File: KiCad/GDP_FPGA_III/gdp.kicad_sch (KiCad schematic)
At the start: 39 parts, among them J1 NKC-Bus, J2 Mini-DIN-6, J3 Mini-DIN-6, J4 AudioJack3, J5 SD_Card, U2 74LVC245, U3 74LVC245, U4 74LVC245

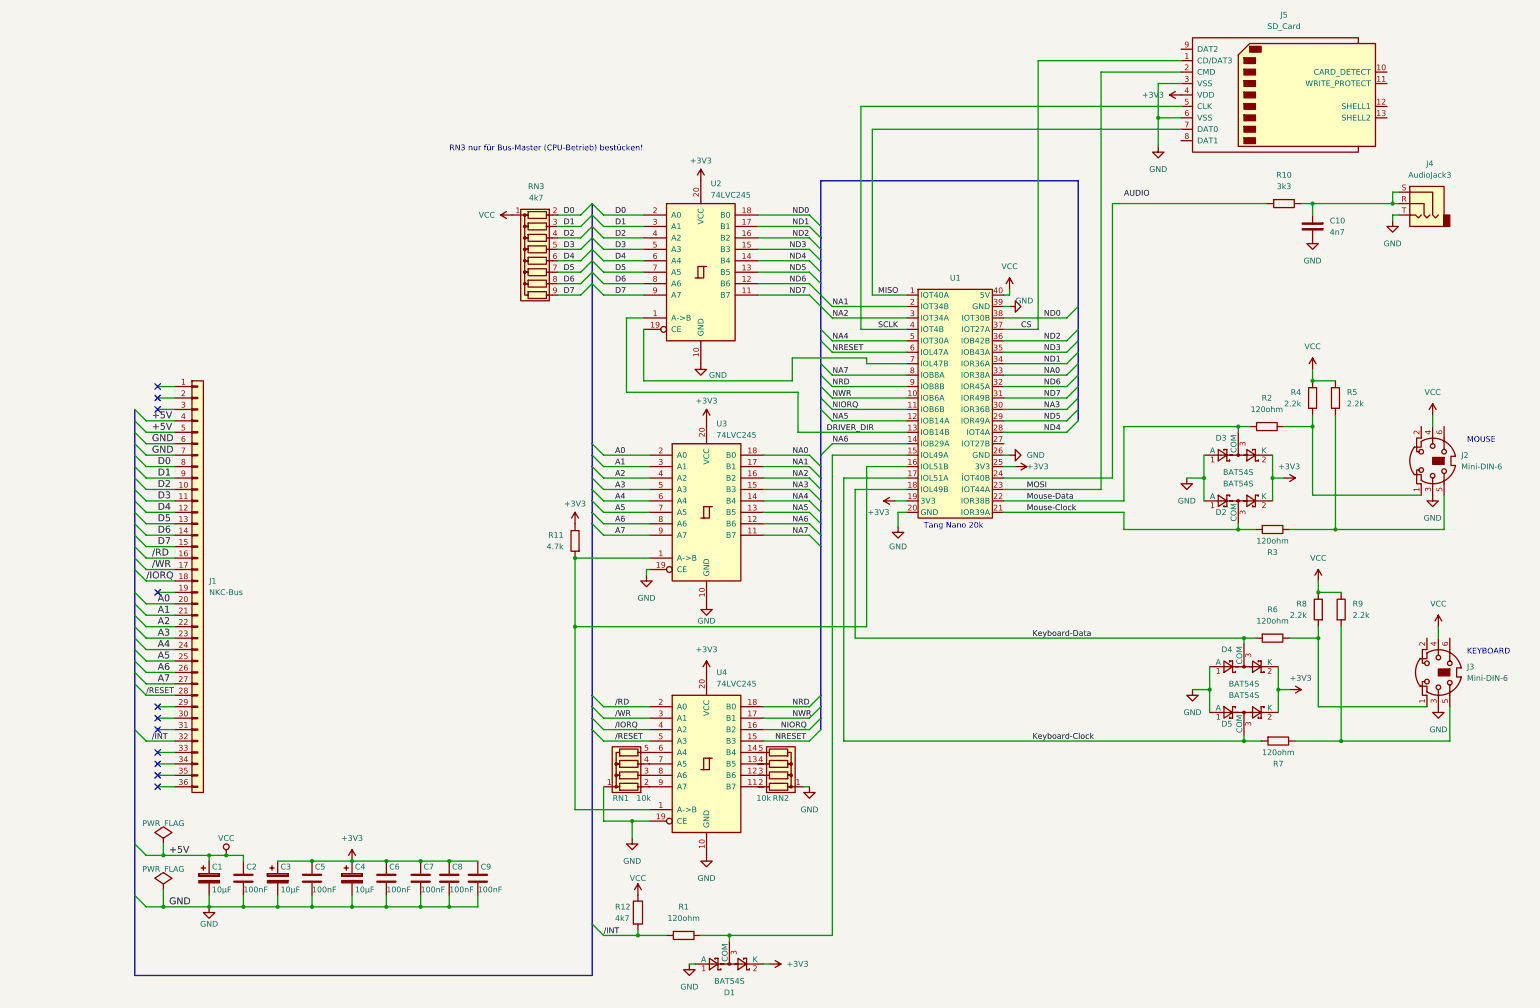
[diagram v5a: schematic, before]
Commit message: update Level shifter to 74LVC8T245
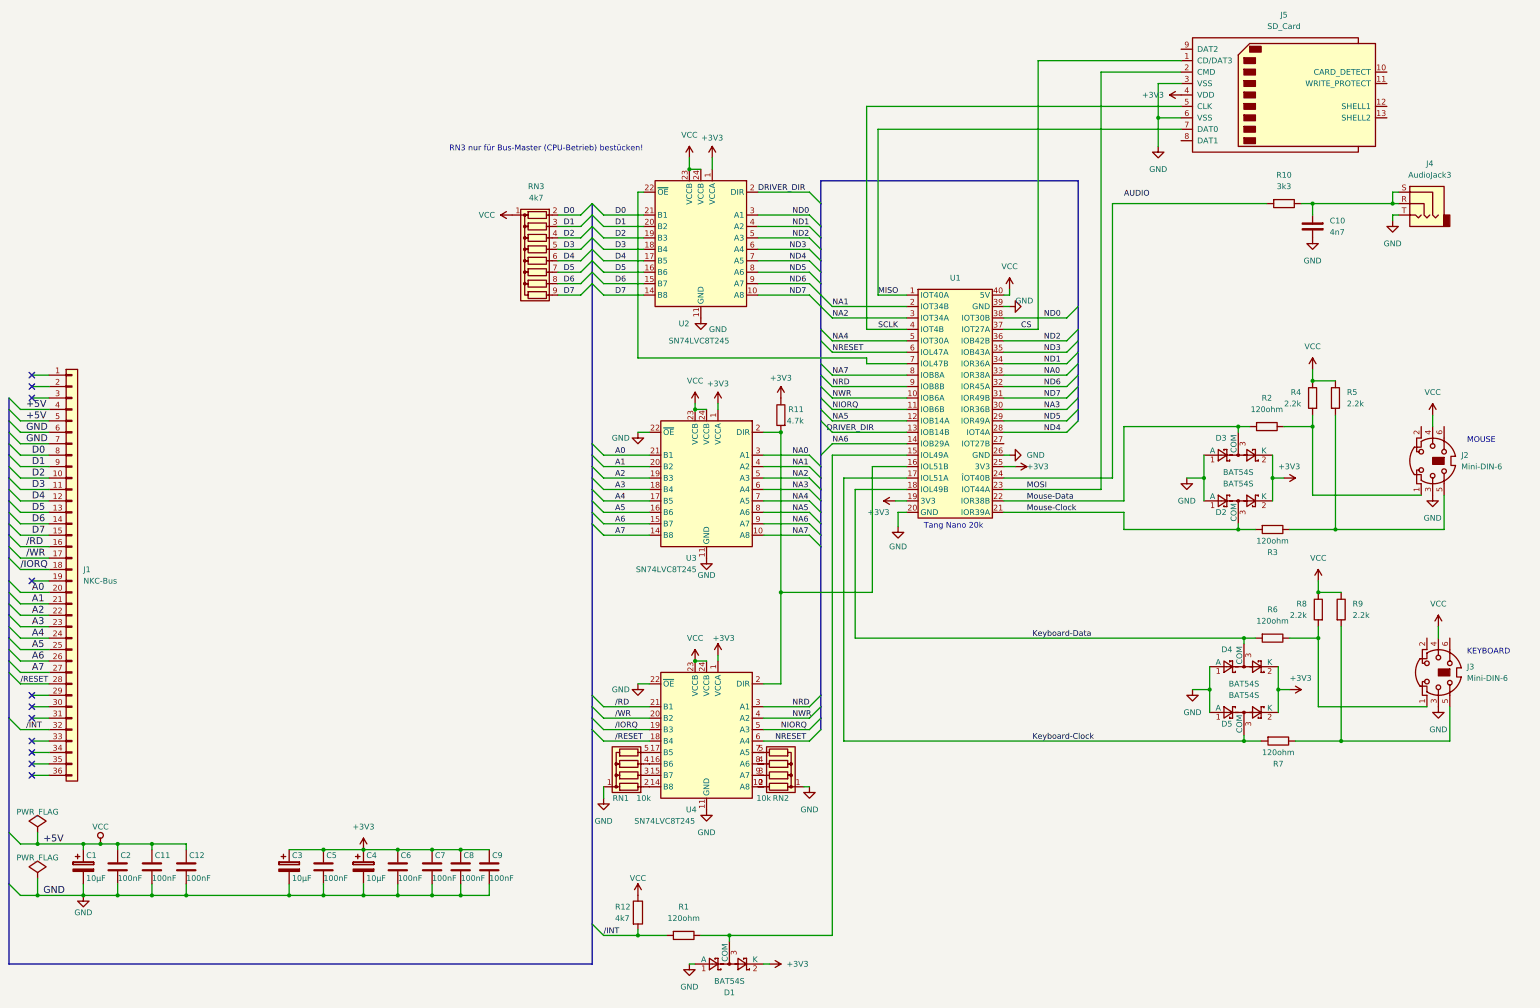
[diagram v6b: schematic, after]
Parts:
- removed U2, U3, U4: 74LVC245, symbol 74xx:74HC245
- added C11, C12: 100nF, Capacitor_THT:C_Disc_D5.0mm_W2.5mm_P5.00mm, symbol ioe_enh-rescue:C
- added U2, U3, U4: SN74LVC8T245, Package_SO:TSSOP-24_4.4x7.8mm_P0.65mm, symbol Logic_LevelTranslator:SN74AVC8T245PW
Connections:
- net +3V3: now also U2.1 (VCCA), U3.1 (VCCA), U4.1 (VCCA)
- net A0: now also U3.21 (B1)
- net A1: now also U3.20 (B2)
- net A2: now also U3.19 (B3)
- net A3: now also U3.18 (B4)
- net A4: now also U3.17 (B5)
- net A5: now also U3.16 (B6)
- net A6: now also U3.15 (B7)
- net A7: now also U3.14 (B8)
- net D0: now also U2.21 (B1)
- net D1: now also U2.20 (B2)
- net D2: now also U2.19 (B3)
- net D3: now also U2.18 (B4)
- net D4: now also U2.17 (B5)
- net D5: now also U2.16 (B6)
- net D6: now also U2.15 (B7)
- net D7: now also U2.14 (B8)
- net DRIVER_DIR: now also U2.2 (DIR); no longer U1.13 (IOB14B)
- net GND: now also C11.2, C12.2, U2.11 (GND), U2.12 (GND), U2.13 (GND), U3.11 (GND), U3.12 (GND), U3.13 (GND), U3.22 (~{OE}), U4.11 (GND), U4.12 (GND), U4.13 (GND), U4.22 (~{OE})
- net NA0: now also U3.3 (A1)
- net NA1: now also U3.4 (A2)
- net NA2: now also U3.5 (A3)
- net NA3: now also U3.6 (A4)
- net NA4: now also U3.7 (A5)
- net NA5: now also U3.8 (A6)
- net NA6: now also U3.9 (A7)
- net NA7: now also U3.10 (A8)
- net ND0: now also U2.3 (A1)
- net ND1: now also U2.4 (A2)
- net ND2: now also U2.5 (A3)
- net ND3: now also U2.6 (A4)
- net ND4: now also U2.7 (A5)
- net ND5: now also U2.8 (A6)
- net ND6: now also U2.9 (A7)
- net ND7: now also U2.10 (A8)
- net NIORQ: now also U4.5 (A3)
- net NRD: now also U4.3 (A1)
- net NRESET: now also U4.6 (A4)
- net NWR: now also U4.4 (A2)
- net VCC: now also C11.1, C12.1, U2.23 (VCCB), U2.24 (VCCB), U3.23 (VCCB), U3.24 (VCCB), U4.23 (VCCB), U4.24 (VCCB)
- net /IORQ: now also U4.19 (B3)
- net /RD: now also U4.21 (B1)
- net /RESET: now also U4.18 (B4)
- net /WR: now also U4.20 (B2)
- net at U1.7 (IOL47B): now also U2.22 (~{OE})
- net at R11.1, U1.16 (IOL51B): now also U3.2 (DIR), U4.2 (DIR)
- net at RN1.5 (R4): now also U4.17 (B5)
- net at RN1.4 (R3): now also U4.16 (B6)
- net at RN1.3 (R2): now also U4.15 (B7)
- net at RN1.2 (R1): now also U4.14 (B8)
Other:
- moved on the sheet: C1, C2, C3, C4, C5, C6, C7, C8, C9, J1, R11

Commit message: Update
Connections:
- net +3V3: no longer R11.2
- net GND: now also R11.2
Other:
- note added: "Slave-Betrieb: U3,U4 Richtung B->A (Datenbus -> Tang-nano) DIR (Pin 2) = 0 Master-Betrieb: U3,U4 Richtung A->B (Tang-nano -> Datenbus) DIR (Pin 2) = 1"
- moved on the sheet: R11
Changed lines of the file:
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@@
   (junction (at 355.6 97.79) (diameter 0) (color 0 0 0 0)
   )
+  (junction (at 257.81 144.78) (diameter 0) (color 0 0 0 0)
+  )
   (junction (at 166.37 201.93) (diameter 0) (color 0 0 0 0)
   )
@@
   (junction (at 332.74 166.37) (diameter 0) (color 0 0 0 0)
   )
-  (junction (at 237.49 109.22) (diameter 0) (color 0 0 0 0)
-  )
   (junction (at 340.36 154.94) (diameter 0) (color 0 0 0 0)
   )
@@
     (stroke (width 0) (type default))
   )
+  (wire (pts (xy 257.81 144.78) (xy 260.35 144.78))
+    (stroke (width 0) (type default))
+  )
   (wire (pts (xy 287.02 81.28) (xy 288.29 81.28))
     (stroke (width 0) (type default))
@@
     (stroke (width 0) (type default))
   )
+  (wire (pts (xy 267.97 144.78) (xy 271.78 144.78))
+    (stroke (width 0) (type default))
+  )
   (wire (pts (xy 355.6 123.19) (xy 355.6 107.95))
     (stroke (width 0) (type default))
@@
     (effects (font (size 1.27 1.27)) (justify left bottom))
   )
+  (text "Slave-Betrieb:  U3,U4 Richtung B->A (Datenbus -> Tang-nano) DIR (Pin 2) = 0\nMaster-Betrieb: U3,U4 Richtung A->B (Tang-nano -> Datenbus) DIR (Pin 2) = 1\n"
+    (at 166.37 27.94 0)
+    (effects (font (size 1.27 1.27)) (justify left bottom))
+  )
   (text "RN3 nur für Bus-Master (CPU-Betrieb) bestücken!" (at 163.83 46.99 0)
     (effects (font (size 1.27 1.27)) (justify left bottom))
@@
     (effects (font (size 1.27 1.27)) (justify left bottom))
   )
+  (symbol (lib_id "power:GND") (at 271.78 144.78 0) (unit 1)
+    (in_bom yes) (on_board yes) (dnp no) (fields_autoplaced)
+    (property "Reference" "#PWR016" (at 271.78 151.13 0)
+      (effects (font (size 1.27 1.27)) hide)
+    )
+    (property "Value" "GND" (at 271.78 149.86 0)
+      (effects (font (size 1.27 1.27)))
+    )
+    (property "Footprint" "" (at 271.78 144.78 0)
+      (effects (font (size 1.27 1.27)) hide)
+    )
+    (property "Datasheet" "" (at 271.78 144.78 0)
+      (effects (font (size 1.27 1.27)) hide)
+    )
+    (pin "1")
+    (instances
+      (project "gdp"
+        (path "/7836164f-f628-443b-9592-71227b3bf791"
+          (reference "#PWR016") (unit 1)
+        )
+      )
+    )
+  )
   (symbol (lib_id "power:GND") (at 382.27 123.19 0) (unit 1)
     (in_bom yes) (on_board yes) (dnp no) (fields_autoplaced)
@@
     )
   )
-  (symbol (lib_id "power:+3V3") (at 237.49 101.6 0) (unit 1)
-    (in_bom yes) (on_board yes) (dnp no) (fields_autoplaced)
-    (property "Reference" "#PWR016" (at 237.49 105.41 0)
-      (effects (font (size 1.27 1.27)) hide)
-    )
-    (property "Value" "+3V3" (at 237.49 97.155 0)
-      (effects (font (size 1.27 1.27)))
-    )
-    (property "Footprint" "" (at 237.49 101.6 0)
-      (effects (font (size 1.27 1.27)) hide)
-    )
-    (property "Datasheet" "" (at 237.49 101.6 0)
-      (effects (font (size 1.27 1.27)) hide)
-    )
-    (pin "1")
-    (instances
-      (project "gdp"
-        (path "/7836164f-f628-443b-9592-71227b3bf791"
-          (reference "#PWR016") (unit 1)
-        )
-      )
-    )
-  )
   (symbol (lib_id "power:VCC") (at 217.17 48.26 0) (unit 1)
     (in_bom yes) (on_board yes) (dnp no) (fields_autoplaced)
@@
     )
   )
-  (symbol (lib_id "PCM_SL_Resistors:2.2k") (at 237.49 105.41 270) (mirror x) (unit 1)
+  (symbol (lib_id "PCM_SL_Resistors:2.2k") (at 264.16 144.78 0) (mirror x) (unit 1)
     (in_bom yes) (on_board yes) (dnp no)
-    (property "Reference" "R11" (at 242.57 104.14 90)
+    (property "Reference" "R11" (at 267.97 147.32 0)
       (effects (font (size 1.27 1.27)) (justify right))
     )
-    (property "Value" "4.7k" (at 242.57 106.68 90)
+    (property "Value" "4.7k" (at 264.16 147.32 0)
       (effects (font (size 1.27 1.27)) (justify right))
     )
-    (property "Footprint" "Resistor_THT:R_Axial_DIN0207_L6.3mm_D2.5mm_P10.16mm_Horizontal" (at 233.172 104.521 0)
+    (property "Footprint" "Resistor_THT:R_Axial_DIN0207_L6.3mm_D2.5mm_P10.16mm_Horizontal" (at 265.049 140.462 0)
       (effects (font (size 1.27 1.27)) hide)
     )
-    (property "Datasheet" "" (at 237.49 104.902 0)
+    (property "Datasheet" "" (at 264.668 144.78 0)
       (effects (font (size 1.27 1.27)) hide)
     )

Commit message: update
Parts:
- U2, U3, U4: value SN74LVC8T245 -> 74LVC8T245 / 74LVXC3245
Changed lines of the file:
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@@
       (effects (font (size 1.27 1.27)) (justify left))
     )
-    (property "Value" "SN74LVC8T245" (at 218.7859 139.7 0)
+    (property "Value" "74LVC8T245 /  74LVXC3245" (at 228.6 143.51 0)
       (effects (font (size 1.27 1.27)) (justify left))
     )
@@
       (effects (font (size 1.27 1.27)) (justify left))
     )
-    (property "Value" "SN74LVC8T245" (at 226.06 88.9 0)
+    (property "Value" "74LVC8T245 /  74LVXC3245" (at 233.68 88.9 0)
       (effects (font (size 1.27 1.27)) (justify left))
     )
@@
       (effects (font (size 1.27 1.27)) (justify left))
     )
-    (property "Value" "SN74LVC8T245" (at 218.44 195.58 0)
-      (effects (font (size 1.27 1.27)) (justify left))
-    )
+    (property "Value" "74LVC8T245 /  74LVXC3245" (at 232.41 200.66 0)
+      (effects (font (size 1.27 1.27)) (justify left))
+    )
